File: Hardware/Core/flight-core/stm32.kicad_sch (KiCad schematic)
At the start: 32 parts, among them J7 Conn_01x04_Socket, SW1 SW_Push, SW2 SW_Push, U1 TCAN1042VDRQ1, U2 STM32G473CCTx, U3 MCP23S17_SS, U4 MAX7221xWG, U5 CC56-12SEKWA, Y1 48 MHz

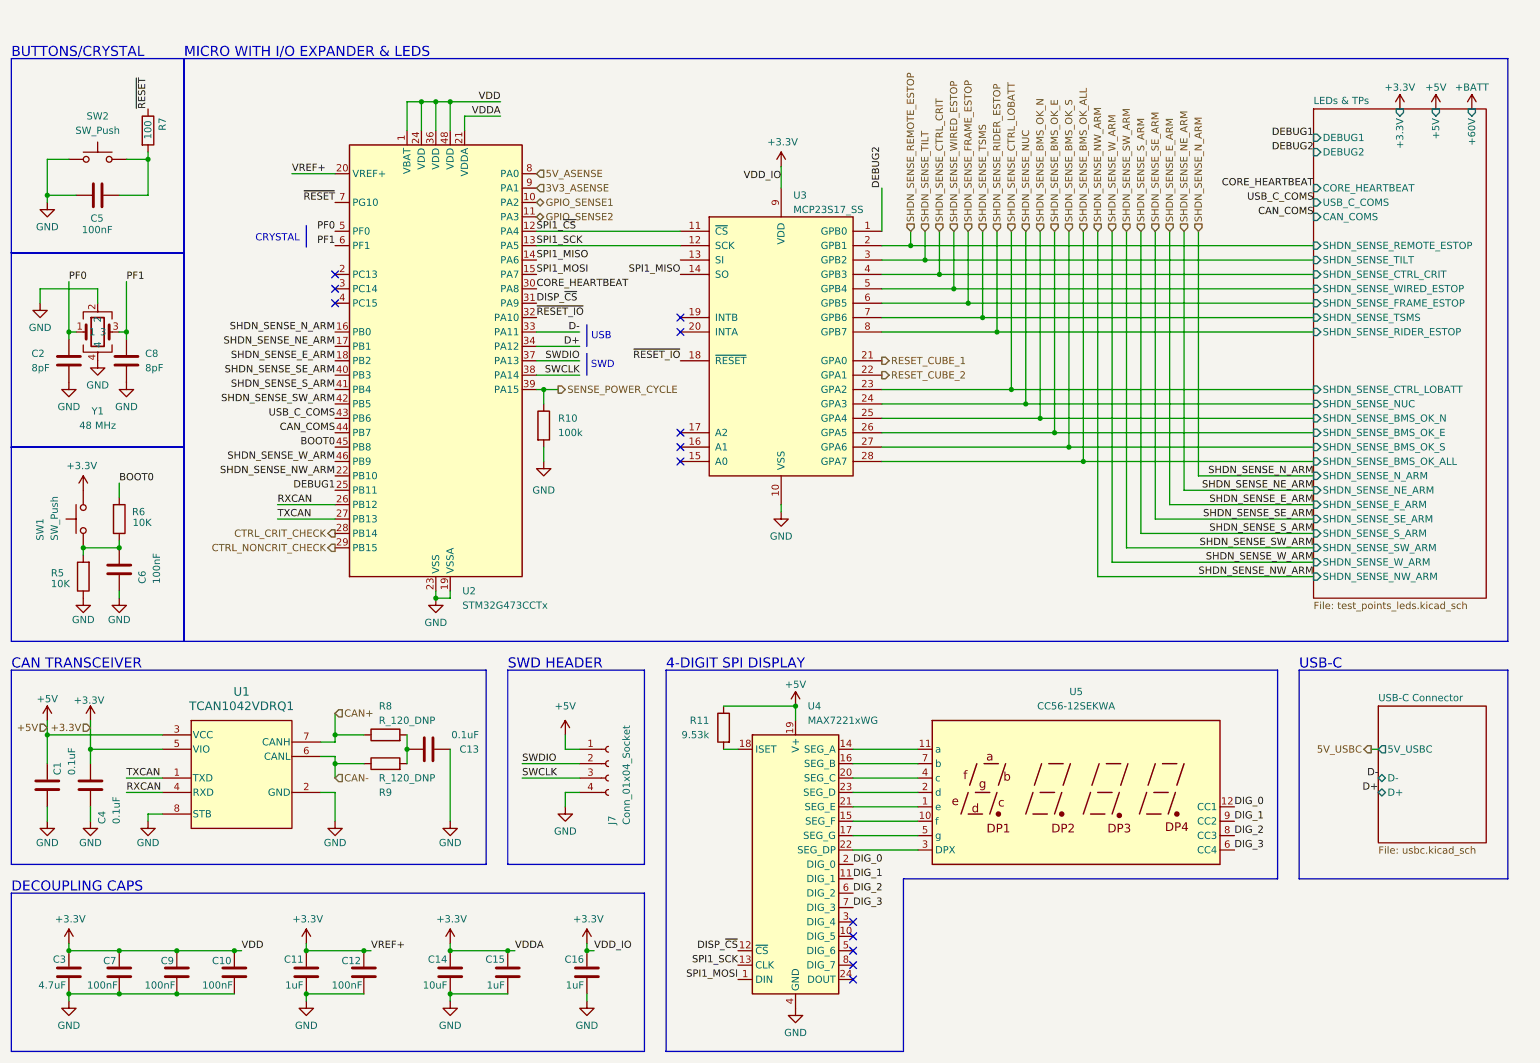
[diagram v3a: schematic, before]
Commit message: major component area placement begun, installing place footprints plugin, updating connectors to vertical
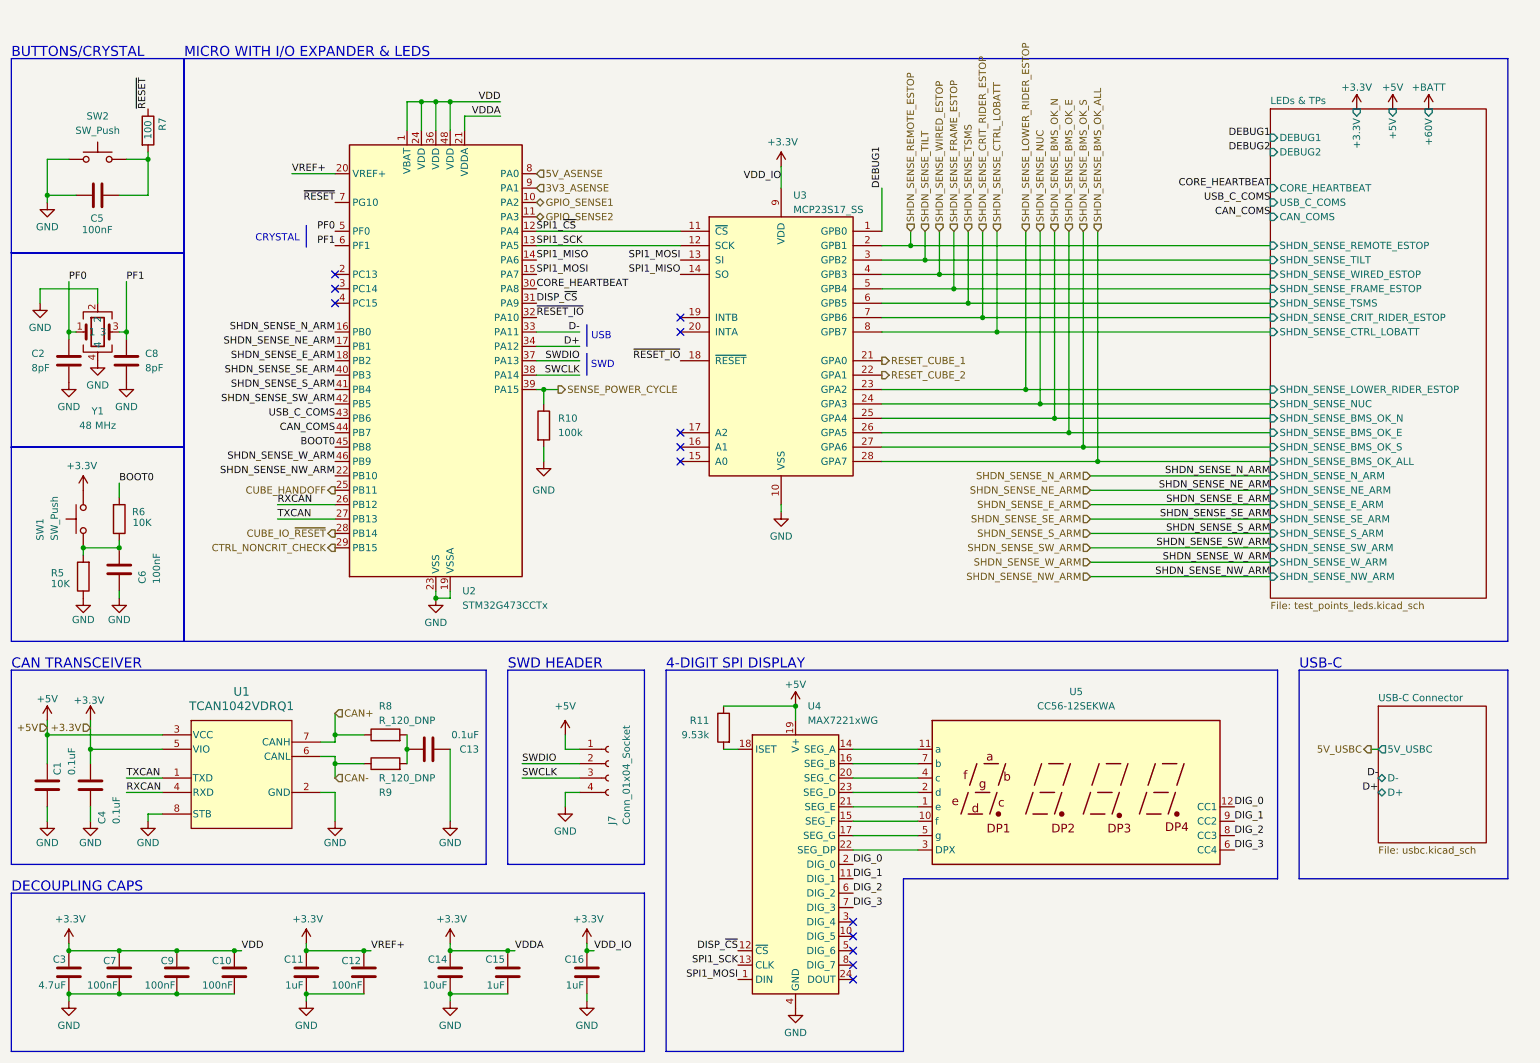
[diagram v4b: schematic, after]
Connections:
- net SHDN_SENSE_CTRL_CRIT is gone; now on net SHDN_SENSE_WIRED_ESTOP: U3.4 (GPB3)
- net SHDN_SENSE_RIDER_ESTOP is gone; now on net SHDN_SENSE_CTRL_LOBATT: U3.8 (GPB7)
- net DEBUG1: now also U3.1 (GPB0); no longer U2.25 (PB11)
- net DEBUG2: no longer U3.1 (GPB0)
- net SHDN_SENSE_CTRL_LOBATT: no longer U3.23 (GPA2)
- net SHDN_SENSE_FRAME_ESTOP: now also U3.5 (GPB4); no longer U3.6 (GPB5)
- net SHDN_SENSE_TSMS: now also U3.6 (GPB5); no longer U3.7 (GPB6)
- net SHDN_SENSE_WIRED_ESTOP: no longer U3.5 (GPB4)
- net SPI1_MOSI: now also U3.13 (SI)
- net CTRL_CRIT_CHECK renamed CUBE_IO_~{RESET}
- new net CUBE_HANDOFF: U2.25 (PB11)
- new net SHDN_SENSE_CRIT_RIDER_ESTOP: U3.7 (GPB6)
- new net SHDN_SENSE_LOWER_RIDER_ESTOP: U3.23 (GPA2)
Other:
- sheet LEDs & TPs ports: added SHDN_SENSE_CRIT_RIDER_ESTOP, SHDN_SENSE_LOWER_RIDER_ESTOP; removed SHDN_SENSE_CTRL_CRIT, SHDN_SENSE_RIDER_ESTOP

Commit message: updated usbc footprint, positioned stm32 peripherals again
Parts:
- R8, R9: footprint footprints:R_0805_OEM -> footprints:R_0603_1608Metric
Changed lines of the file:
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@@
 			)
 		)
-		(property "Footprint" "footprints:R_0805_OEM"
+		(property "Footprint" "footprints:R_0603_1608Metric"
 			(at 78.74 173.99 0)
 			(effects
@@
 			)
 		)
-		(property "Footprint" "footprints:R_0805_OEM"
+		(property "Footprint" "footprints:R_0603_1608Metric"
 			(at 78.74 168.91 0)
 			(effects

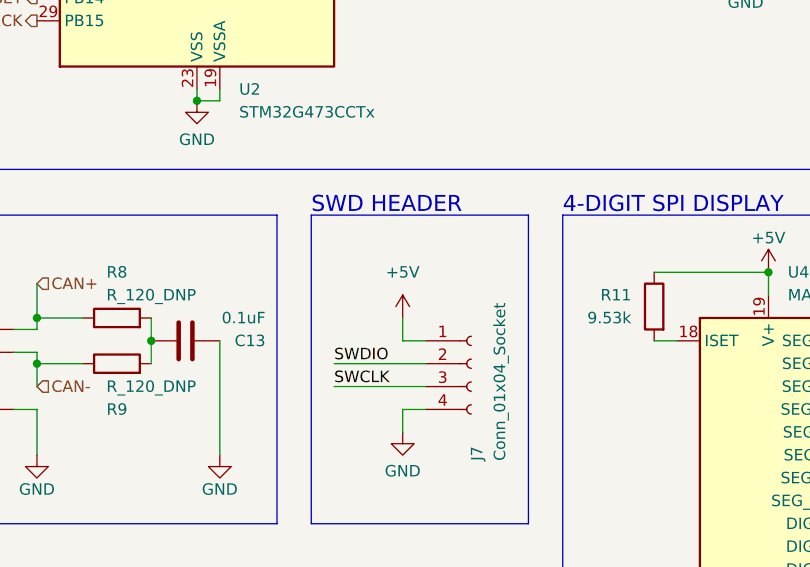
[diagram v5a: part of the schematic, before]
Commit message: swapped 5 & 6 in bus arb, placed components
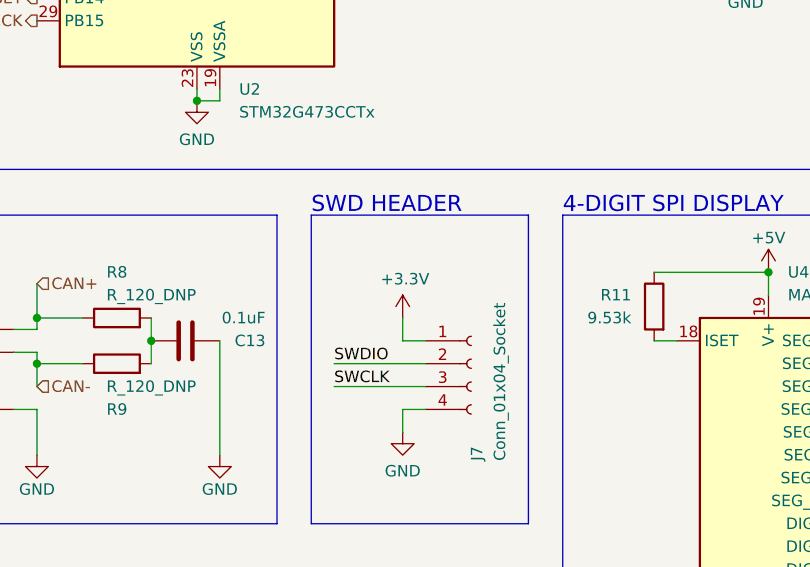
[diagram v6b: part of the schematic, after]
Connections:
- net +3.3V: now also J7.1 (Pin_1)
- net +5V: no longer J7.1 (Pin_1)
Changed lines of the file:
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@@
+	)
+	(symbol
+		(lib_id "power:+3.3V")
+		(at 114.3 138.43 0)
+		(mirror y)
+		(unit 1)
+		(exclude_from_sim no)
+		(in_bom yes)
+		(on_board yes)
+		(dnp no)
+		(property "Reference" "#PWR038"
+			(at 114.3 142.24 0)
+			(effects
+				(font
+					(size 1.27 1.27)
+				)
+				(hide yes)
+			)
+		)
+		(property "Value" "+3.3V"
+			(at 114.554 134.112 0)
+			(effects
+				(font
+					(size 1.27 1.27)
+				)
+			)
+		)
+		(property "Footprint" ""
+			(at 114.3 138.43 0)
+			(effects
+				(font
+					(size 1.27 1.27)
+				)
+				(hide yes)
+			)
+		)
+		(property "Datasheet" ""
+			(at 114.3 138.43 0)
+			(effects
+				(font
+					(size 1.27 1.27)
+				)
+				(hide yes)
+			)
+		)
+		(property "Description" "Power symbol creates a global label with name \"+3.3V\""
+			(at 114.3 138.43 0)
+			(effects
+				(font
+					(size 1.27 1.27)
+				)
+				(hide yes)
+			)
+		)
+		(pin "1"
+		)
+		(instances
+			(project "flight-core"
+				(path "/93f46f4b-cdf5-47ec-af03-96378e73b2e1/91e18f07-bd3f-4576-bbe1-a0227cf7132e"
+					(reference "#PWR038")
+					(unit 1)
+				)
+			)
+		)
 	)
 	(symbol
@@
 					(unit 1)
 				)
-			)
-		)
-	)
-	(symbol
-		(lib_name "+5V_1")
-		(lib_id "power:+5V")
-		(at 114.3 138.43 0)
-		(unit 1)
-		(exclude_from_sim no)
-		(in_bom yes)
-		(on_board yes)
-		(dnp no)
-		(property "Reference" "#PWR038"
-			(at 114.3 142.24 0)
-			(effects
-				(font
-					(size 1.27 1.27)
-				)
-				(hide yes)
-			)
-		)
-		(property "Value" "+5V"
-			(at 114.3 133.35 0)
-			(effects
-				(font
-					(size 1.27 1.27)
-				)
-			)
-		)
-		(property "Footprint" ""
-			(at 114.3 138.43 0)
-			(effects
-				(font
-					(size 1.27 1.27)
-				)
-				(hide yes)
-			)
-		)
-		(property "Datasheet" ""
-			(at 114.3 138.43 0)
-			(effects
-				(font
-					(size 1.27 1.27)
-				)
-				(hide yes)
-			)
-		)
-		(property "Description" "Power symbol creates a global label with name \"+5V\""
-			(at 114.3 138.43 0)
-			(effects
-				(font
-					(size 1.27 1.27)
-				)
-				(hide yes)
-			)
-		)
-		(pin "1"
-		)
-		(instances
-			(project "flight-core"
-				(path "/93f46f4b-cdf5-47ec-af03-96378e73b2e1/91e18f07-bd3f-4576-bbe1-a0227cf7132e"
-					(reference "#PWR038")
-					(unit 1)
-				)

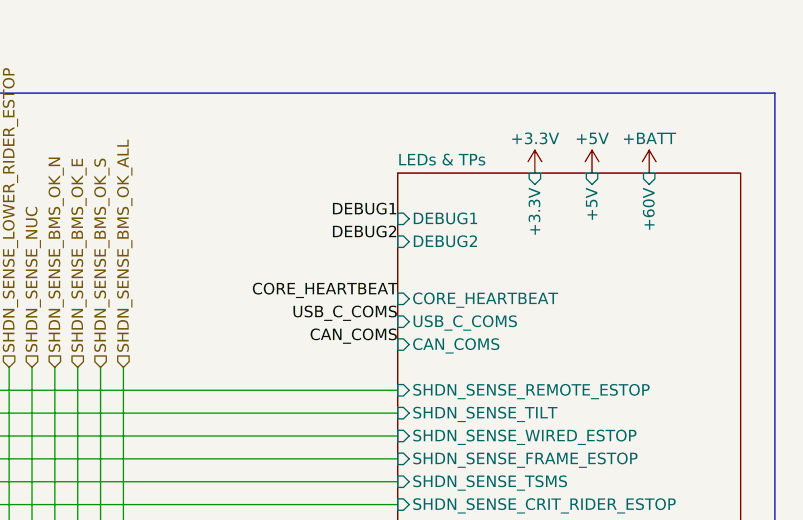
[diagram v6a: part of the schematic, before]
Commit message: removed extra test points, removed debug2, reannotated schem
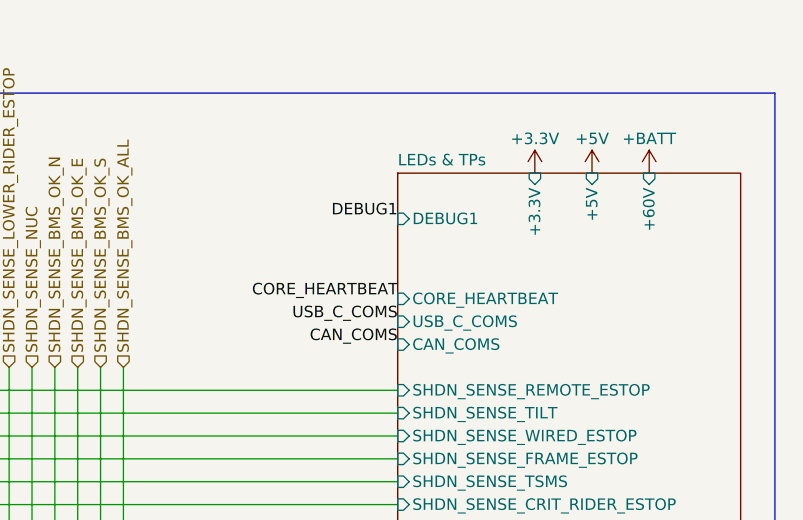
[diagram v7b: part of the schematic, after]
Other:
- sheet LEDs & TPs ports: added none; removed DEBUG2
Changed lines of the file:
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@@
 		)
 	)
-	(label "DEBUG2"
-		(at 238.76 35.56 180)
-		(effects
-			(font
-				(size 1.27 1.27)
-			)
-			(justify right bottom)
-		)
-	)
 	(label "CORE_HEARTBEAT"
 		(at 238.76 41.91 180)
@@
 			(effects
 				(font
-					(size 1.27 1.27)
-				)
-				(justify left)
-			)
-		)
-		(pin "DEBUG2" input
-			(at 238.76 35.56 180)
-			(effects
-				(font

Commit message: routing stm32
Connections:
- net DEBUG1: now also U3.21 (GPA0); no longer U3.1 (GPB0)
- net RESET_CUBE_1: now also U3.1 (GPB0); no longer U3.21 (GPA0)
- net SHDN_SENSE_BMS_OK_ALL: now also U3.25 (GPA4); no longer U3.28 (GPA7)
- net SHDN_SENSE_BMS_OK_E: now also U3.27 (GPA6); no longer U3.26 (GPA5)
- net SHDN_SENSE_BMS_OK_N: now also U3.28 (GPA7); no longer U3.25 (GPA4)
- net SHDN_SENSE_BMS_OK_S: now also U3.26 (GPA5); no longer U3.27 (GPA6)
- net SHDN_SENSE_LOWER_RIDER_ESTOP: now also U3.24 (GPA3); no longer U3.23 (GPA2)
- net SHDN_SENSE_NUC: now also U3.23 (GPA2); no longer U3.24 (GPA3)
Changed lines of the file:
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@@
 	)
 	(label "DEBUG1"
-		(at 170.18 41.91 90)
+		(at 170.18 72.39 0)
 		(effects
 			(font
@@
 	(hierarchical_label "SHDN_SENSE_LOWER_RIDER_ESTOP"
 		(shape input)
-		(at 195.58 49.53 90)
+		(at 198.12 49.53 90)
 		(effects
 			(font
@@
 	(hierarchical_label "SHDN_SENSE_BMS_OK_N"
 		(shape input)
-		(at 200.66 49.53 90)
+		(at 208.28 49.53 90)
 		(effects
 			(font
@@
 	(hierarchical_label "SHDN_SENSE_NUC"
 		(shape input)
-		(at 198.12 49.53 90)
+		(at 195.58 49.53 90)
 		(effects
 			(font
@@
 	(hierarchical_label "SHDN_SENSE_BMS_OK_S"
 		(shape input)
-		(at 205.74 49.53 90)
+		(at 203.2 49.53 90)
 		(effects
 			(font
@@
 	(hierarchical_label "SHDN_SENSE_BMS_OK_E"
 		(shape input)
-		(at 203.2 49.53 90)
+		(at 205.74 49.53 90)
 		(effects
 			(font
@@
 	(hierarchical_label "SHDN_SENSE_BMS_OK_ALL"
 		(shape input)
-		(at 208.28 49.53 90)
+		(at 200.66 49.53 90)
 		(effects
 			(font
@@
 	(hierarchical_label "RESET_CUBE_1"
 		(shape output)
-		(at 170.18 72.39 0)
-		(effects
-			(font
+		(at 170.18 41.91 90)
+		(effects
+			(font
